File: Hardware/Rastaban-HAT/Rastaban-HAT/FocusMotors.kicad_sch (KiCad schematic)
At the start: 10 parts, among them U7 DRV8838 POLOLU, U8 TLV1117-33

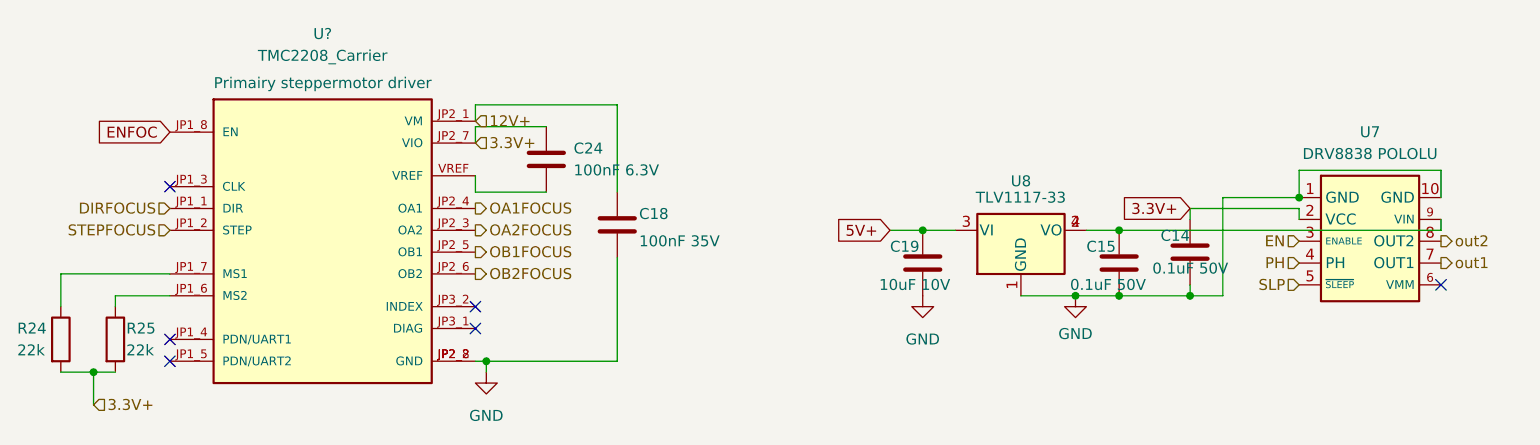
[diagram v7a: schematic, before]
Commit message: finished drv8838 implementation for PCBNEW
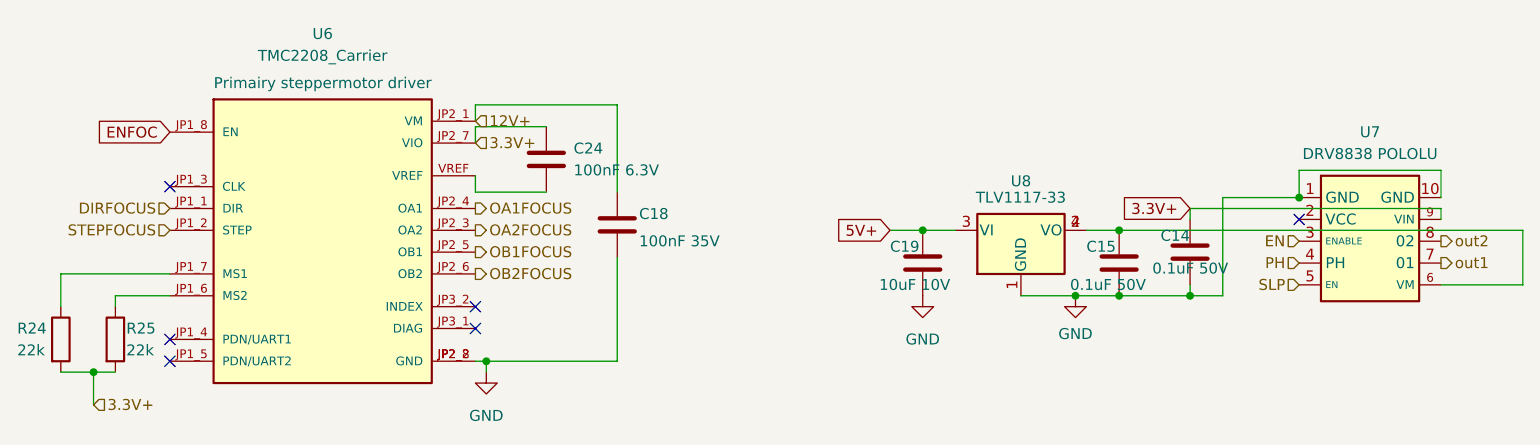
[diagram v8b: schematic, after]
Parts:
- U7: footprint (none) -> Module:DRV8838 POLOLU
- gave numbers to parts that had none: 1
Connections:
- net 3.3V+: now also U7.9 (VIN); no longer U7.2 (VCC)
- net at U7.6 (VM): now also C15.2, U8.2 (VO), U8.4 (VO)
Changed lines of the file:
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@@
   )
   (no_connect (at 118.11 116.205))
+  (no_connect (at 213.995 106.045))
   (no_connect (at 82.55 120.015))
   (no_connect (at 118.11 118.745))
   (no_connect (at 82.55 122.555))
   (no_connect (at 82.55 102.235))
-  (no_connect (at 230.505 113.665))
   (wire (pts (xy 213.995 100.33) (xy 213.995 103.505))
     (stroke (width 0) (type default) (color 0 0 0 0))
@@
     (stroke (width 0) (type default) (color 0 0 0 0))
   )
-  (wire (pts (xy 193.04 107.315) (xy 189.23 107.315))
-    (stroke (width 0) (type default) (color 0 0 0 0))
-  )
   (wire (pts (xy 193.04 114.935) (xy 201.295 114.935))
     (stroke (width 0) (type default) (color 0 0 0 0))
@@
     (stroke (width 0) (type default) (color 0 0 0 0))
   )
+  (wire (pts (xy 240.03 107.315) (xy 240.03 113.665))
+    (stroke (width 0) (type default) (color 0 0 0 0))
+  )
   (wire (pts (xy 82.55 112.395) (xy 69.85 112.395))
     (stroke (width 0) (type default) (color 0 0 0 0))
   )
-  (wire (pts (xy 201.295 104.775) (xy 213.995 104.775))
+  (wire (pts (xy 230.505 104.775) (xy 230.505 106.045))
+    (stroke (width 0) (type default) (color 0 0 0 0))
+  )
+  (wire (pts (xy 201.295 104.775) (xy 230.505 104.775))
     (stroke (width 0) (type default) (color 0 0 0 0))
   )
@@
     (stroke (width 0) (type default) (color 0 0 0 0))
   )
-  (wire (pts (xy 213.995 104.775) (xy 213.995 106.045))
+  (wire (pts (xy 240.03 113.665) (xy 230.505 113.665))
     (stroke (width 0) (type default) (color 0 0 0 0))
   )
@@
     (stroke (width 0) (type default) (color 0 0 0 0))
   )
-  (wire (pts (xy 193.04 107.315) (xy 230.505 107.315))
+  (wire (pts (xy 193.04 107.315) (xy 240.03 107.315))
     (stroke (width 0) (type default) (color 0 0 0 0))
   )
@@
     (stroke (width 0) (type default) (color 0 0 0 0))
   )
+  (wire (pts (xy 189.23 107.315) (xy 193.04 107.315))
+    (stroke (width 0) (type default) (color 0 0 0 0))
+  )
   (wire (pts (xy 170.18 107.315) (xy 173.99 107.315))
     (stroke (width 0) (type default) (color 0 0 0 0))
   )
   (wire (pts (xy 119.38 122.555) (xy 118.11 122.555))
-    (stroke (width 0) (type default) (color 0 0 0 0))
-  )
-  (wire (pts (xy 230.505 106.045) (xy 230.505 107.315))
     (stroke (width 0) (type default) (color 0 0 0 0))
   )
@@
     (property "Reference" "U7" (id 0) (at 222.25 95.885 0))
     (property "Value" "DRV8838 POLOLU" (id 1) (at 222.25 98.425 0))
-    (property "Footprint" "" (id 2) (at 226.695 130.81 0)
+    (property "Footprint" "Module:DRV8838 POLOLU" (id 2) (at 226.695 130.81 0)
       (effects (font (size 1.27 1.27)) hide)
     )
@@
   (symbol (lib_name "TMC2208_SILENTSTEPSTICK_1") (lib_id "TMC2208_SILENTSTEPSTICK:TMC2208_SILENTSTEPSTICK") (at 100.33 109.855 0) (unit 1)
     (in_bom yes) (on_board yes)
-    (property "Reference" "U?" (id 0) (at 100.33 84.455 0))
+    (property "Reference" "U6" (id 0) (at 100.33 84.455 0))
     (property "Value" "TMC2208_Carrier" (id 1) (at 100.33 86.995 0))
     (property "Footprint" "SnapEDA Library:MODULE_TMC2208_SILENTSTEPSTICK" (id 2) (at 85.09 128.905 0)
